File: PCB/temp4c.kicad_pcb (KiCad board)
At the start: 2 copper layers, 98 x 50 mm, 40 parts, among them J1 10-24VAC, J2 USB_IN, J3 eflashy32, J4 THERMO1, J5 THERMO2, J6 THERMO3, J7 THERMO4, U1 VXO7803-500, U2 ESP32-WROOM-32D, U3 SHT35-DISB, U4 MAX31855KASA, U5 MAX31855KASA, U6 MAX31855KASA, U7 MAX31855KASA

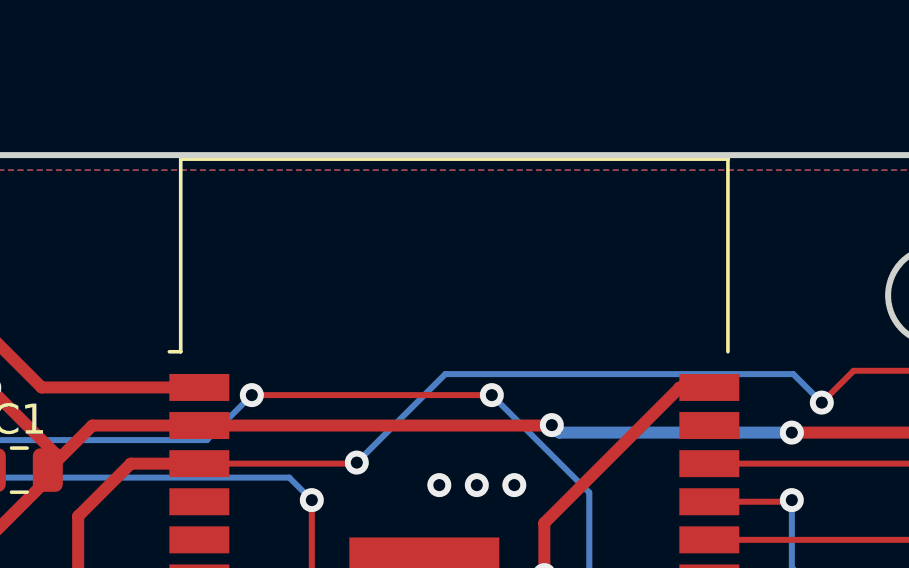
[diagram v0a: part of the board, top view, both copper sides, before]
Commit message: order number silkscreen
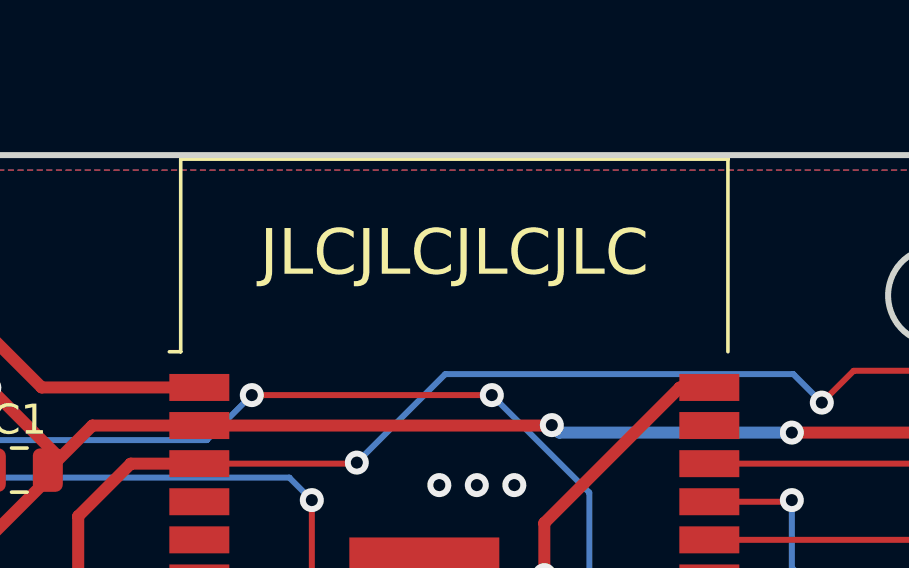
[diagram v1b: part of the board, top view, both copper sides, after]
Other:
- board text added: "JLCJLCJLCJLC"
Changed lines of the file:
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@@
   (gr_line (start 43.75 55.75) (end 38 55.75) (layer "Edge.Cuts") (width 0.2))
   (gr_circle (center 122.56 38.68) (end 124.16 38.68) (layer "Edge.Cuts") (width 0.2) (fill none))
+  (gr_text "JLCJLCJLCJLC" (at 106.5 37.25) (layer "F.SilkS")
+    (effects (font (size 1.524 1.524) (thickness 0.2)))
+  )
   (segment (start 102.75 70.25) (end 104.45 70.25) (width 0.2) (layer "F.Cu") (net 1))
   (segment (start 73.35 38.335) (end 73.35 44.6) (width 0.4) (layer "F.Cu") (net 1))

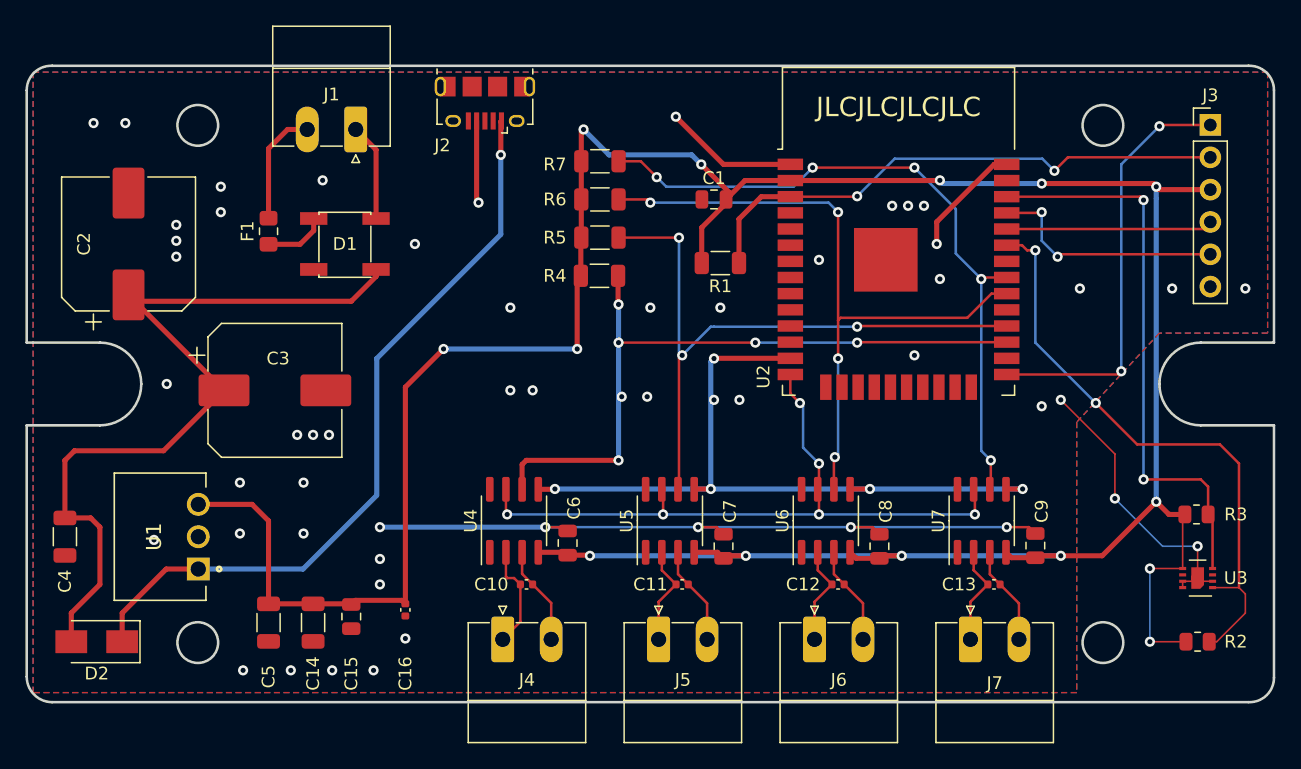
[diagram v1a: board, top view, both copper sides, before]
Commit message: switch rectifier
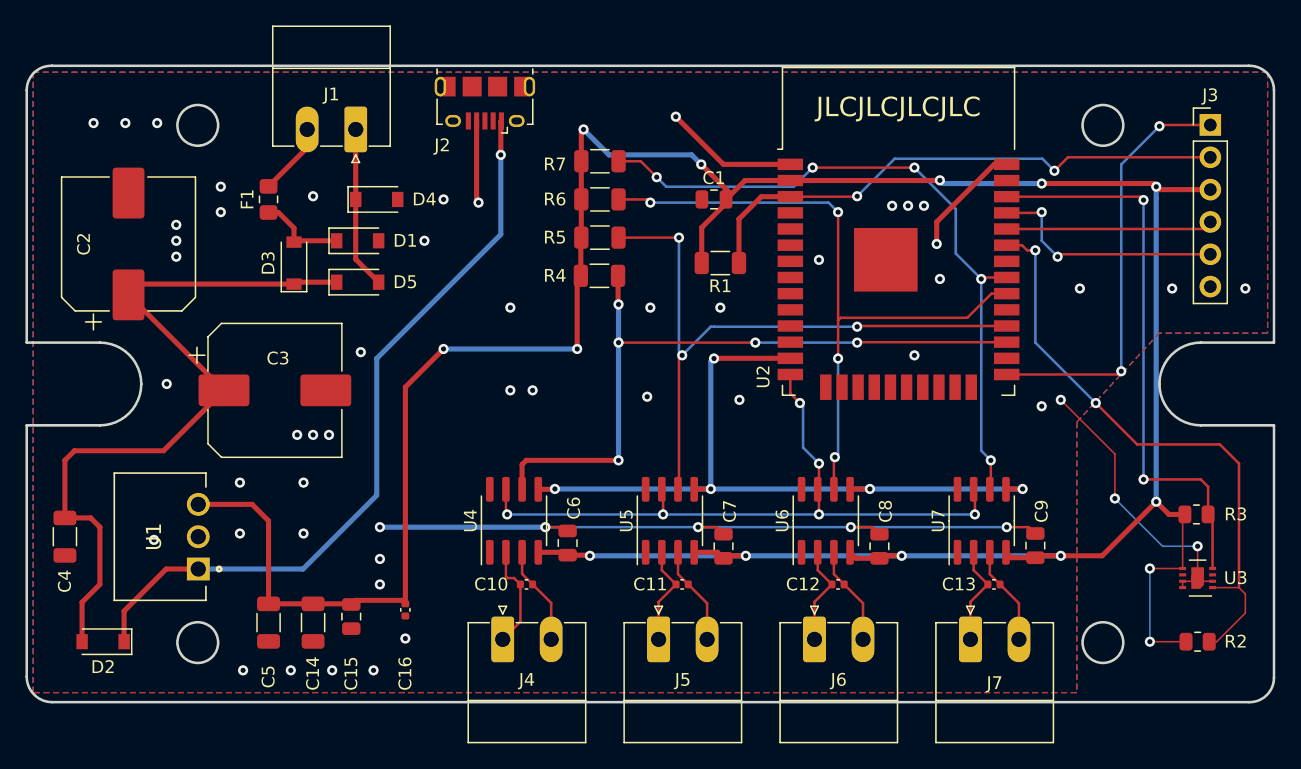
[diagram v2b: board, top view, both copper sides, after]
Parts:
- added D3: B5819, Diode_SMD:D_SOD-123, F.Cu at (59.0, 49.5)
- added D4: B5819, Diode_SMD:D_SOD-123, F.Cu at (65.5, 44.5)
- added D5: B5819, Diode_SMD:D_SOD-123, F.Cu at (64.0, 51.0)
- D1: value MB10S -> B5819; footprint Diode_SMD:Diode_Bridge_DiodesInc_MBS -> Diode_SMD:D_SOD-123
- D2: value SS14 -> B5819; footprint Diode_SMD:D_SMA -> Diode_SMD:D_SOD-123
- moved F1 2.50 mm to (57.0, 44.5)
- moved D1 1.03 mm to (64.0, 47.8), turned to 0 degrees
- moved D2 0.50 mm to (44.0, 79.2)
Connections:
- D1 pad 1: Net-(C2-Pad1) -> Net-(F1-Pad1)
- F1 pad 1: Net-(D1-Pad4) -> Net-(F1-Pad1)
- J1 pad 1: Net-(D1-Pad3) -> Net-(J1-Pad1)
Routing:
- net Net-(J1-Pad1): track 0.00 -> 12.7 mm
- net Net-(D1-Pad3): track 7.66 -> 0.00 mm
- net Net-(F1-Pad1): track 0.00 -> 7.00 mm
- net Net-(D1-Pad4): track 4.95 -> 0.00 mm
- net Net-(C2-Pad1): track 63.9 -> 59.3 mm
- net Net-(J1-Pad2): track 9.14 -> 5.73 mm
- net GND: vias 55 -> 56

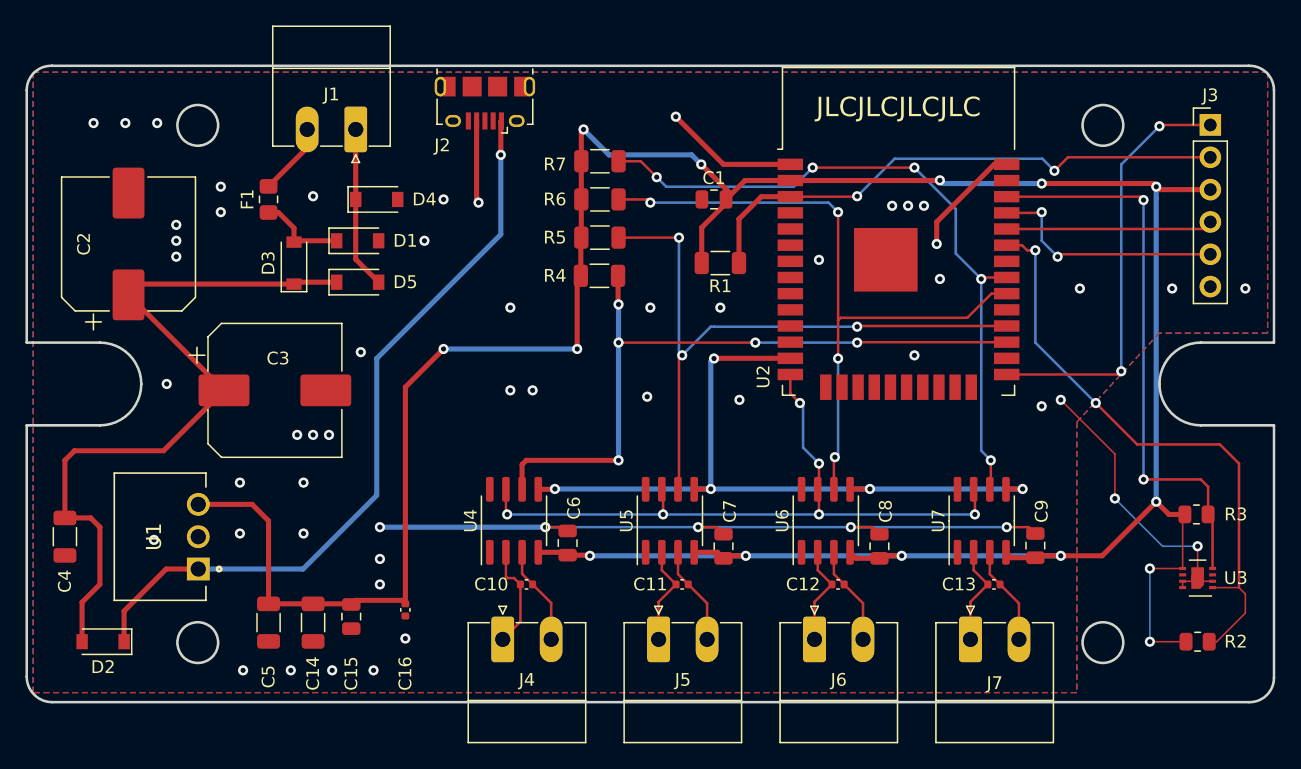
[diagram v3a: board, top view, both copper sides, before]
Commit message: esptemp8c rename
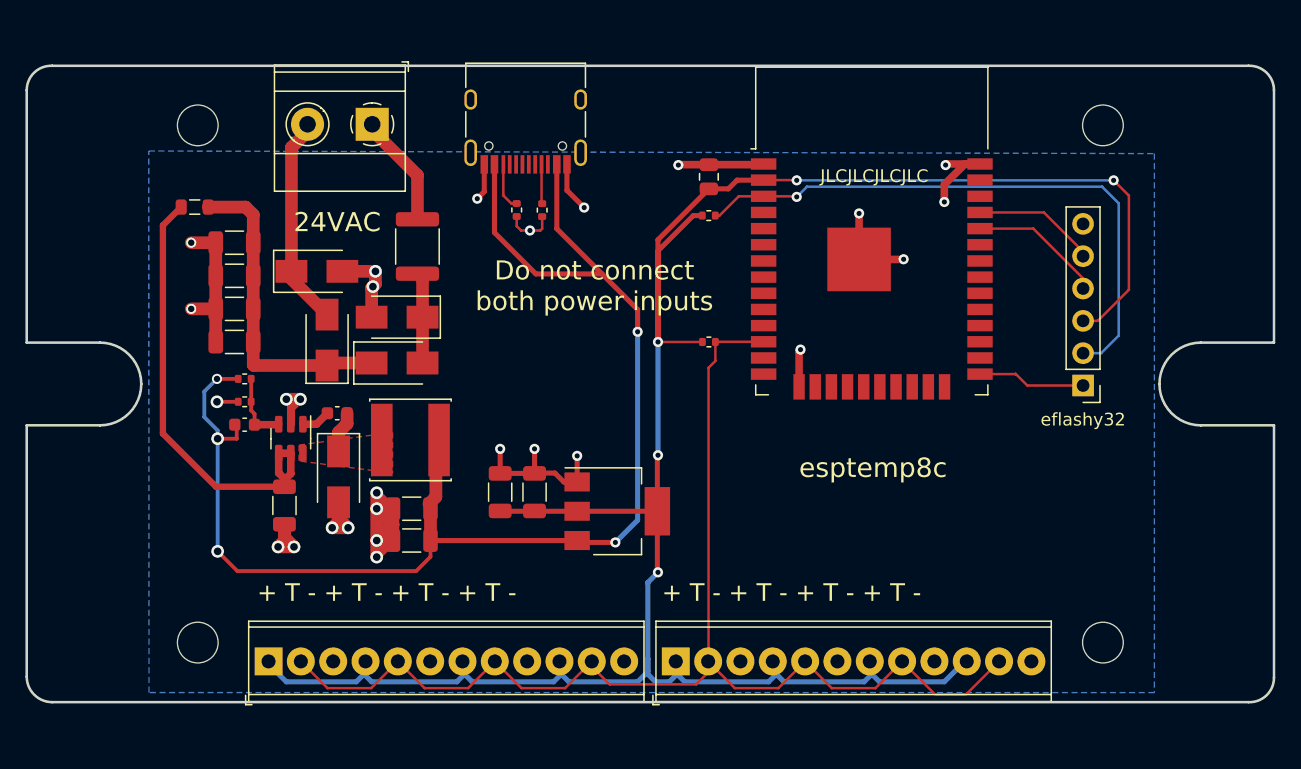
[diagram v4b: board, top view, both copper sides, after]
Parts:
- removed C13, C16: 10nF, Capacitor_SMD:C_0402_1005Metric
- removed C14: 10uF 50V, Capacitor_SMD:C_1206_3216Metric
- removed C15: 0.1uF, Capacitor_SMD:C_0805_2012Metric
- removed J6: THERMO3, Connector_Phoenix_MC:PhoenixContact_MC_1,5_2-G-3.81_1x02_P3.81mm_Horizontal
- removed J7: THERMO4, Connector_Phoenix_MC:PhoenixContact_MC_1,5_2-G-3.81_1x02_P3.81mm_Horizontal
- removed R7: 10k, Resistor_SMD:R_1206_3216Metric
- removed the U1 at (51.5, 73.5)
- removed U4, U5, U6, U7: MAX31855KASA, Package_SO:SOIC-8_3.9x4.9mm_P1.27mm
- added FB1: 600@100MHz, Inductor_SMD:L_0805_2012Metric, F.Cu at (51.2, 45.1)
- added H1: MountingHole, MountingHole:MountingHole_3.2mm_M3, F.Cu at (51.4, 79.3)
- added H2: MountingHole, MountingHole:MountingHole_3.2mm_M3, F.Cu at (122.6, 79.3)
- added H3: MountingHole, MountingHole:MountingHole_3.2mm_M3, F.Cu at (51.4, 38.7)
- added H4: MountingHole, MountingHole:MountingHole_3.2mm_M3, F.Cu at (122.6, 38.7)
- added L1: 6.8uH, Inductor_SMD:L_Sunlord_SWPA60xxS, F.Cu at (68.2, 63.4)
- added U2: BD9G101G, Package_TO_SOT_SMD:SOT-23-6, F.Cu at (58.8, 63.3)
- C10: value 10nF -> 0.1uF 50V; footprint Capacitor_SMD:C_0402_1005Metric -> Capacitor_SMD:C_0603_1608Metric
- C11, C12: value 10nF -> 10uF 50V; footprint Capacitor_SMD:C_0402_1005Metric -> Capacitor_SMD:C_1206_3216Metric
- C2: value 220uF 50V -> 15nF; footprint Capacitor_SMD:CP_Elec_10x10 -> Capacitor_SMD:C_0603_1608Metric
- C3: value 220uF 50V -> 10uF 50V; footprint Capacitor_SMD:CP_Elec_10x10 -> Capacitor_SMD:C_1206_3216Metric
- C6, C7: value 0.1uF/10V -> 10uF 50V; footprint Capacitor_SMD:C_0805_2012Metric -> Capacitor_SMD:C_1206_3216Metric
- C8, C9: value 0.1uF/10V -> 47u; footprint Capacitor_SMD:C_0805_2012Metric -> Capacitor_SMD:C_1206_3216Metric
- D1, D2, D3, D4, D5: value B5819 -> SS210; footprint Diode_SMD:D_SOD-123 -> Diode_SMD:D_SMA
- F1: value 0ZCK0050FF2E (TLC-PSMD050) -> 140mA hold / 340mA trip mSMD014; footprint Fuse:Fuse_0805_2012Metric_Pad1.15x1.40mm_HandSolder -> Fuse:Fuse_1812_4532Metric
- J1: value 10-24VAC -> Probes; footprint Connector_Phoenix_MC:PhoenixContact_MC_1,5_2-G-3.81_1x02_P3.81mm_Horizontal -> TerminalBlock_Phoenix:TerminalBlock_Phoenix_MPT-0,5-12-2.54_1x12_P2.54mm_Horizontal
- J2: value USB_IN -> Probes; footprint Connector_USB:USB_Micro-B_Amphenol_10118194_Horizontal -> TerminalBlock_Phoenix:TerminalBlock_Phoenix_MPT-0,5-12-2.54_1x12_P2.54mm_Horizontal
- J4: value THERMO1 -> 24VAC; footprint Connector_Phoenix_MC:PhoenixContact_MC_1,5_2-G-3.81_1x02_P3.81mm_Horizontal -> TerminalBlock_Phoenix:TerminalBlock_Phoenix_MKDS-1,5-2-5.08_1x02_P5.08mm_Horizontal
- J5: value THERMO2 -> USB_C_Receptacle_USB2.0; footprint Connector_Phoenix_MC:PhoenixContact_MC_1,5_2-G-3.81_1x02_P3.81mm_Horizontal -> Connector_USB:USB_C_Receptacle_HRO_TYPE-C-31-M-12
- R1: footprint Resistor_SMD:R_1206_3216Metric -> Resistor_SMD:R_0402_1005Metric
- R2: value 10k -> 5k1; footprint Resistor_SMD:R_0805_2012Metric -> Resistor_SMD:R_0402_1005Metric
- R3: value 10k -> 3k9; footprint Resistor_SMD:R_0805_2012Metric -> Resistor_SMD:R_0402_1005Metric
- R4: value 10k -> 680; footprint Resistor_SMD:R_1206_3216Metric -> Resistor_SMD:R_0402_1005Metric
- R5, R6: value 10k -> 5k1; footprint Resistor_SMD:R_1206_3216Metric -> Resistor_SMD:R_0402_1005Metric
- U3: value SHT35-DISB -> AMS1117-3.3; footprint Sensor_Humidity:Sensirion_DFN-8-1EP_2.5x2.5mm_P0.5mm_EP1.1x1.7mm -> Package_TO_SOT_SMD:SOT-223-3_TabPin2
- moved R3 75.5 mm to (55.1, 58.6), turned to 180 degrees
- moved C9 49.1 mm to (68.2, 68.8), turned to 180 degrees
- moved J2 46.4 mm to (89.0, 80.8), turned to 0 degrees
- moved U3 45.9 mm to (84.4, 69.0), turned to 0 degrees
- moved R2 45.0 mm to (91.6, 55.7)
- moved J5 42.7 mm to (77.2, 37.7), turned to 180 degrees
- moved J1 42.4 mm to (57.0, 80.8), turned to 0 degrees
- moved J4 41.8 mm to (65.1, 38.6), turned to 180 degrees
- moved C8 36.8 mm to (68.2, 71.3), turned to 180 degrees
- moved C7 34.6 mm to (58.2, 68.5)
- moved C6 30.6 mm to (54.3, 55.7), turned to 180 degrees
- moved C5 30.0 mm to (54.3, 47.9), turned to 180 degrees
- moved R4 29.6 mm to (55.1, 60.4)
- moved D2 29.5 mm to (61.6, 55.5), turned to 90 degrees
- moved C12 27.5 mm to (75.2, 67.5), turned to 90 degrees
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- renumbered U2 to U1
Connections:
- C1 pad 2: +3V3 -> 3V3
- C10 pad 1: Net-(C10-Pad1) -> +5V
- C10 pad 2: Net-(C10-Pad2) -> /Power Section/FB
- C11 pad 1: Net-(C11-Pad1) -> 3V3
- C11 pad 2: Net-(C11-Pad2) -> GND
- C12 pad 1: Net-(C12-Pad1) -> 3V3
- C12 pad 2: Net-(C12-Pad2) -> GND
- C2 pad 2: GND -> /Power Section/LX
- C3 pad 1: Net-(C2-Pad1) -> /Power Section/Vrec
- C4 pad 1: Net-(C2-Pad1) -> /Power Section/Vrec
- C5 pad 1: +3V3 -> /Power Section/Vrec
- C6 pad 1: GND -> /Power Section/Vrec
- C6 pad 2: +3V3 -> GND
- C7 pad 1: GND -> Net-(C7-Pad1)
- C7 pad 2: +3V3 -> GND
- C8 pad 1: GND -> +5V
- C8 pad 2: +3V3 -> GND
- C9 pad 1: GND -> +5V
- C9 pad 2: +3V3 -> GND
- D1 pad 1: Net-(F1-Pad1) -> Net-(J4-Pad2)
- D2 pad 1: 5VUSB -> /Power Section/Vrec
- D2 pad 2: Net-(C2-Pad1) -> Net-(J4-Pad2)
- D3 pad 1: Net-(C2-Pad1) -> Net-(D3-Pad1)
- D3 pad 2: Net-(F1-Pad1) -> GND
- D4 pad 1: Net-(J1-Pad1) -> /Power Section/Vrec
- D4 pad 2: GND -> Net-(D3-Pad1)
- D5 pad 1: Net-(C2-Pad1) -> /Power Section/LX
- D5 pad 2: Net-(J1-Pad1) -> GND
- F1 pad 1: Net-(F1-Pad1) -> Net-(J4-Pad1)
- F1 pad 2: Net-(J1-Pad2) -> Net-(D3-Pad1)
- J1 pad 1: Net-(J1-Pad1) -> 3V3
- J1 pad 2: Net-(J1-Pad2) -> PROBE_BUS
- J2 pad 1: 5VUSB -> 3V3
- J2 pad 2: unconnected-(J2-Pad2) -> PROBE_BUS
- J2 pad 3: unconnected-(J2-Pad3) -> GND
- J2 pad 4: GND -> 3V3
- J2 pad 5: unconnected-(J2-Pad5) -> PROBE_BUS
- J2 pad 6: (no net) -> GND
- J3 pad 3: +3V3 -> 3V3
- J4 pad 1: Net-(C10-Pad2) -> Net-(J4-Pad1)
- J4 pad 2: Net-(C10-Pad1) -> Net-(J4-Pad2)
- R1 pad 2: +3V3 -> 3V3
- R2 pad 1: +3V3 -> 3V3
- R2 pad 2: I2C_SDA -> PROBE_BUS
- R3 pad 1: +3V3 -> /Power Section/FB
- R3 pad 2: I2C_SCL -> +5V
- R4 pad 1: +3V3 -> GND
- R4 pad 2: CS1 -> /Power Section/FB
- R5 pad 1: +3V3 -> Net-(J5-PadA5)
- R5 pad 2: CS2 -> GND
- R6 pad 1: +3V3 -> Net-(J5-PadB5)
- R6 pad 2: CS3 -> GND
- U1 pad 12: unconnected-(U2-Pad12) -> PROBE_BUS
- U1 pad 13: HSPI_CLK -> unconnected-(U1-Pad13)
- U1 pad 14: HSPI_MISO -> unconnected-(U1-Pad14)
- U1 pad 16: HSPI_MOSI -> unconnected-(U1-Pad16)
- U1 pad 2: +3V3 -> 3V3
- U1 pad 23: HSPI_CS -> unconnected-(U1-Pad23)
- U1 pad 27: CS1 -> unconnected-(U1-Pad27)
- U1 pad 28: CS2 -> unconnected-(U1-Pad28)
- U1 pad 30: CS3 -> unconnected-(U1-Pad30)
- U1 pad 31: CS4 -> unconnected-(U1-Pad31)
- U1 pad 33: I2C_SDA -> unconnected-(U1-Pad33)
- U1 pad 36: I2C_SCL -> unconnected-(U1-Pad36)
- U3 pad 1: I2C_SDA -> GND
- U3 pad 2: GND -> 3V3
- U3 pad 3: unconnected-(U3-Pad3) -> +5V
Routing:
- net +3V3: track 238.3 -> 0.00 mm, vias 14 -> 0
- net 3V3: track 0.00 -> 180.9 mm, vias 0 -> 5
- net +5V: track 0.00 -> 107.2 mm, vias 0 -> 5
- net PROBE_BUS: track 0.00 -> 97.1 mm
- net 5VUSB: track 59.5 -> 0.00 mm, vias 1 -> 0
- net HSPI_CLK: track 58.6 -> 0.00 mm, vias 5 -> 0
- net Net-(C2-Pad1): track 59.3 -> 2.28 mm
- net HSPI_MISO: track 54.8 -> 0.00 mm, vias 6 -> 0
- net CS1: track 54.7 -> 0.00 mm, vias 5 -> 0
- net CS4: track 54.5 -> 0.00 mm, vias 5 -> 0
- net CS3: track 53.7 -> 0.00 mm, vias 4 -> 0
- net CS2: track 51.2 -> 0.00 mm, vias 3 -> 0
- net I2C_SDA: track 47.4 -> 0.00 mm, vias 2 -> 0
- net I2C_SCL: track 44.7 -> 0.00 mm, vias 2 -> 0
- net Net-(C7-Pad1): track 0.00 -> 35.1 mm
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- added copper zone on F.Cu, net /Power Section/LX
- removed copper zone on F.Cu, net GND
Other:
- outline, holes or cut-outs redrawn
- board text added: "+ T - + T - + T - + T -"
- board text added: "24VAC"
- board text added: "Case : Hammond 1593VBK"
- board text added: "Do not connect both power inputs"
- board text added: "eflashy32"
- board text added: "esptemp8c"
